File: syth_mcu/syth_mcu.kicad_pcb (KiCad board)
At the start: 2 copper layers, 154 x 117 mm, 97 parts, among them J10 Conn_01x20, J11 Conn_01x20, J3 PJ-320A, J4 Conn_01x04, J5 Conn_01x20, J6 Conn_01x20, J7 Conn_01x16, J8 Conn_01x08, SW1 SW_Push, SW10 Solder, SW11 SW_DIP_x03, SW13 Solder, SW2 SW_Push, SW3 SW_Push, SW4 SW_Push, SW5 SW_Push, SW6 SW_Push, SW7 SS12D10, SW8 Solder, SW9 Solder, U1 LM358, U4 AMS1117-3.3, U5 TFT_320x240

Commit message: System check, DRC runs
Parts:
- added C6: 1uF, Capacitor_THT:C_Disc_D5.0mm_W2.5mm_P5.00mm, F.Cu at (134.7, 65.5)
- moved C14 8.43 mm to (64.7, 103.8), turned to 180 degrees
- moved C16 4.46 mm to (201.1, 105.1)
- moved D11 3.20 mm to (193.7, 128.2)
- moved D8 3.20 mm to (193.6, 124.3)
- moved RightConn1 2.02 mm to (61.9, 137.1)
- moved LeftConn1 1.05 mm to (202.8, 137.1)
- moved G*** 0.85 mm to (107.7, 155.5)
- moved SW11 0.68 mm to (123.0, 56.0)
- moved USB1 0.13 mm to (67.8, 52.4)
- moved J3 0.10 mm to (89.2, 49.7)
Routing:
- net D_5V: track 422.3 -> 461.9 mm
- net GND: track 0.00 -> 28.1 mm, vias 5 -> 21
- net AMS2_3.3V: track 359.2 -> 382.5 mm
- net PB8: track 118.7 -> 111.9 mm
- net PB9: track 98.4 -> 91.6 mm
- net /MuxAnalog/C6: track 156.7 -> 150.1 mm
- net Net-(5V_On1-K): track 0.00 -> 4.32 mm
- net Net-(C4-Pad1): track 0.00 -> 3.52 mm
- net MCU5V: track 36.5 -> 39.7 mm
- net PB6: track 214.7 -> 217.1 mm
- net /DAC Channel/DAC Left PWM: track 0.00 -> 2.36 mm
- net /DAC Channel/DAC Right PWM: track 0.00 -> 2.34 mm, vias 0 -> 1
- net PC14: track 154.3 -> 156.3 mm
- net /MuxAnalog/C1: track 144.9 -> 146.7 mm, vias 3 -> 4
- net /MuxAnalog/C5: track 82.9 -> 84.6 mm, vias 2 -> 3
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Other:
- board text added: "3V3"
- board text added: "5V"
- board text added: "C0"
- board text added: "Free/extern"
- board text added: "Join main 5V with MCU"
- board text added: "SIG"
- board text removed: "Join USB 5V with MCU"

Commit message: add screw, removed serial rev.pol diode
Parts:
- removed D1: SS34, Diode_SMD:D_SMA
- added H13: MountingHole, MountingHole:MountingHole_3.2mm_M3, F.Cu at (131.7, 60.6)
- added H14: MountingHole, MountingHole:MountingHole_3.2mm_M3, F.Cu at (73.6, 155.5)
- added H15: MountingHole, MountingHole:MountingHole_3.2mm_M3, F.Cu at (139.3, 155.5)
- moved SW13 0.38 mm to (104.5, 66.5)
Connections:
- AMS3.3VFused1 pad 2: AMS2_3.3V -> (no net)
- F3 pad 2: Net-(D1-A) -> D_5V
- GND1 pad 2: GND -> (no net)
- GND2 pad 2: GND -> (no net)
- USB5VFused1 pad 2: D_5V -> (no net)
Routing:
- net Net-(D1-A): track 4.01 -> 0.00 mm
- added copper zone on F.Cu, net D_5V
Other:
- board text added: "Reg 3.3V for LM358"
- board text added: "VCC"

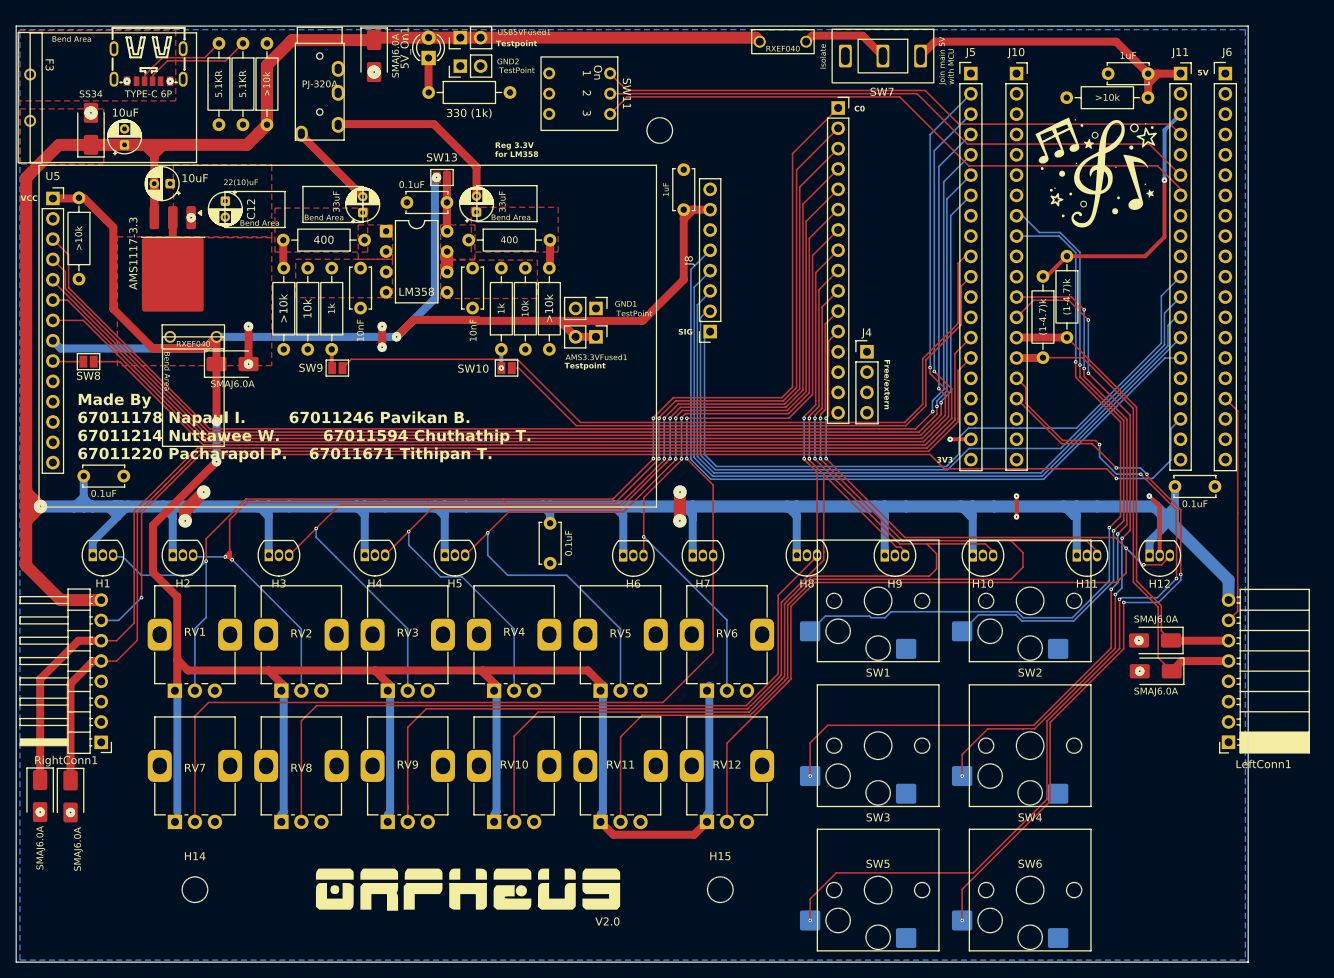
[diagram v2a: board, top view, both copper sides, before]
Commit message: pcb: switch footprint to Cherry MX hotswap, reroute traces
- Replace Kailh Choc V1 hotswap footprints with Cherry MX compatible footprints
- Adjust switch spacing and reroute affected traces for new footprint geometry
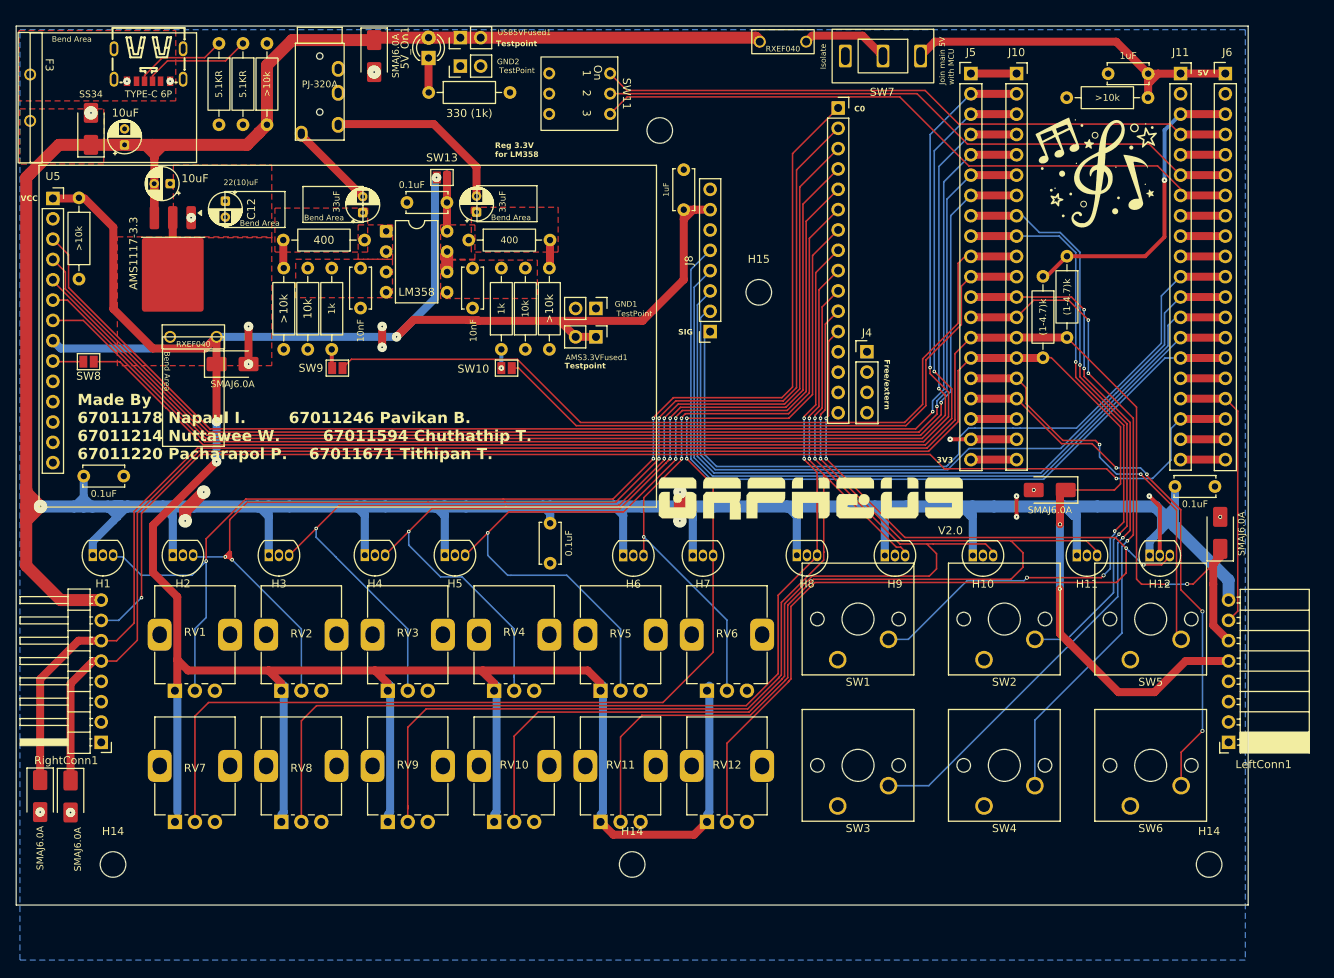
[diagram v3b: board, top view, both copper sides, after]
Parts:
- added H14: MountingHole, MountingHole:MountingHole_3.2mm_M3, F.Cu at (200.4, 152.3)
- added H14: MountingHole, MountingHole:MountingHole_3.2mm_M3, F.Cu at (128.3, 152.3)
- SW1, SW2, SW3, SW4, SW5, SW6: footprint Switch_Keyboard_Hotswap_Kailh:SW_Hotswap_Kailh_Choc_V1_1.00u -> Button_Switch_Keyboard:SW_Cherry_MX_1.00u_PCB
- moved H15 74.8 mm to (144.1, 80.8)
- moved G*** 65.0 mm to (150.6, 106.6)
- moved SW5 42.7 mm to (190.5, 126.8)
- moved D11 26.3 mm to (180.4, 105.5)
- moved SW6 16.3 mm to (190.5, 145.0)
- moved D8 15.7 mm to (201.8, 110.9), turned to 90 degrees
- moved H14 10.7 mm to (63.4, 152.3)
- moved SW4 9.49 mm to (172.2, 145.0)
- moved SW2 9.34 mm to (172.2, 126.8)
- moved SW3 9.08 mm to (153.9, 145.0)
- moved SW1 8.92 mm to (153.9, 126.8)
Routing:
- net PB8: track 111.9 -> 51.0 mm, vias 5 -> 2
- net PB7: track 214.7 -> 237.8 mm, vias 0 -> 2
- net PB9: track 91.6 -> 68.9 mm, vias 5 -> 4
- net PB6: track 217.1 -> 229.7 mm, vias 0 -> 2
- net 3V3: track 33.4 -> 45.4 mm
- net MCU5V: track 39.7 -> 51.0 mm
- net PB4: track 101.1 -> 92.2 mm, vias 5 -> 3
- net PA8: track 157.2 -> 162.9 mm
- net PB3: track 74.2 -> 79.9 mm
- net PB15: track 157.7 -> 163.4 mm
- net PB14: track 153.8 -> 159.5 mm
- net PB13: track 163.0 -> 168.7 mm
- net PB12: track 0.00 -> 5.71 mm
- net PA9: track 153.2 -> 159.0 mm
- net PA15: track 98.6 -> 104.3 mm
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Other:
- board size 154 x 117 mm -> 154 x 109.9 mm

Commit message: pcb: Gateron hotswap footprint (marbastlib KS-2P02) + route J4-J7 pins
- SW1-SW6: replace Cherry MX PCB solder footprint with
  PCM_marbastlib-mx:SW_MX_HS_KS-2P02B01-01_1u for hotswap socket support
- Route Net-(J4-Pin_1..4) connecting J4.1-4 to J7.13-16
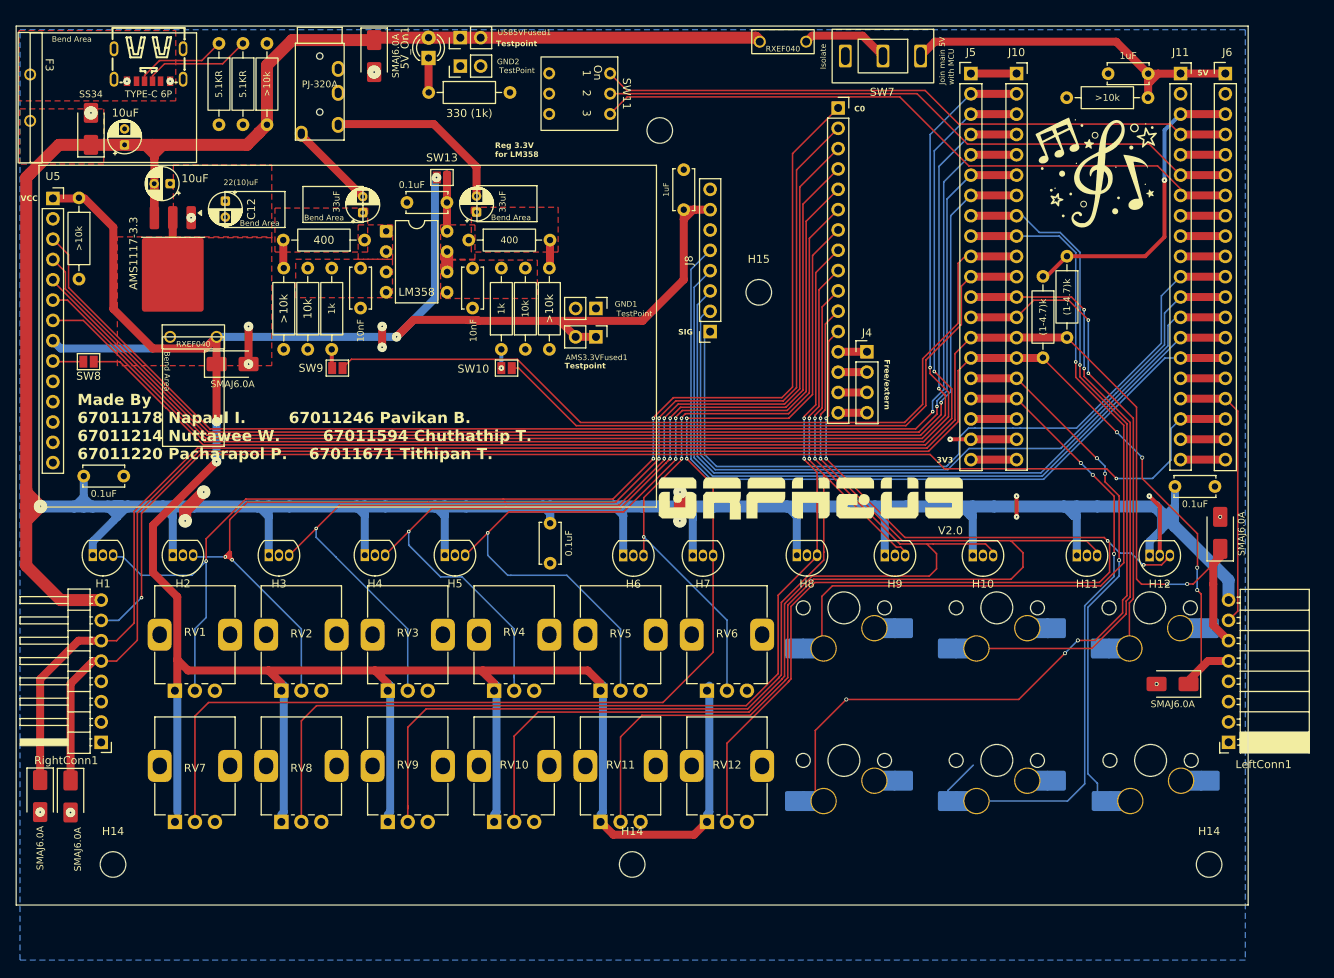
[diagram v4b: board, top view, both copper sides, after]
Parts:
- SW1, SW2, SW3, SW4, SW5, SW6: footprint Button_Switch_Keyboard:SW_Cherry_MX_1.00u_PCB -> PCM_marbastlib-mx:SW_MX_HS_KS-2P02B01-01_1u; moved to B.Cu
- moved SW4 32.3 mm to (192.9, 120.3), turned to 0 degrees
- moved SW3 31.8 mm to (173.8, 120.3), turned to 0 degrees
- moved D11 28.7 mm to (195.8, 129.8)
- moved SW2 21.6 mm to (154.7, 139.3), turned to 0 degrees
- moved SW6 17.6 mm to (173.8, 139.3), turned to 0 degrees
- moved SW5 12.8 mm to (193.1, 139.3), turned to 0 degrees
- moved SW1 6.53 mm to (154.7, 120.3), turned to 0 degrees
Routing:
- net PA11: track 73.5 -> 117.0 mm, vias 2 -> 4
- net PB7: track 237.8 -> 217.5 mm, vias 2 -> 4
- net PB5: track 82.2 -> 65.2 mm, vias 3 -> 2
- net PB4: track 92.2 -> 75.9 mm, vias 3 -> 2
- net PB8: track 51.0 -> 66.2 mm, vias 2 -> 3
- net PA12: track 88.1 -> 101.3 mm, vias 4 -> 1
- net PB9: track 68.9 -> 80.6 mm, vias 4 -> 3
- net Net-(J4-Pin_4): track 0.00 -> 3.60 mm
- net Net-(J4-Pin_2): track 0.00 -> 3.60 mm
- net Net-(J4-Pin_3): track 0.00 -> 3.60 mm
- net Net-(J4-Pin_1): track 0.00 -> 3.60 mm
- net /MuxAnalog/C11: track 142.8 -> 141.7 mm
